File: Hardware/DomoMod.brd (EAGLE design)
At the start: 80 x 30 mm, 9 parts, among them Q1 BSS138, Q2 BSS138

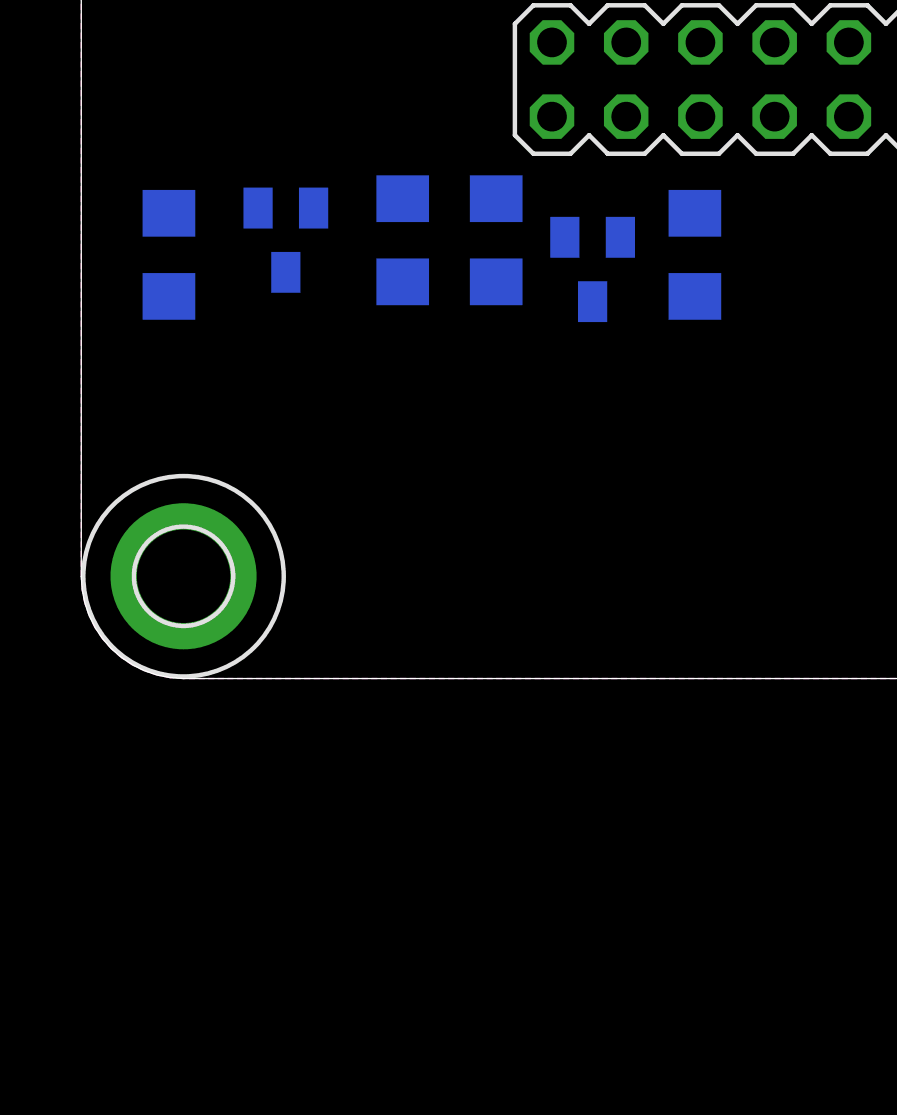
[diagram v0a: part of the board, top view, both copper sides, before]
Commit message: Added schematics for Temp/Hum and barometric pressure sensor.
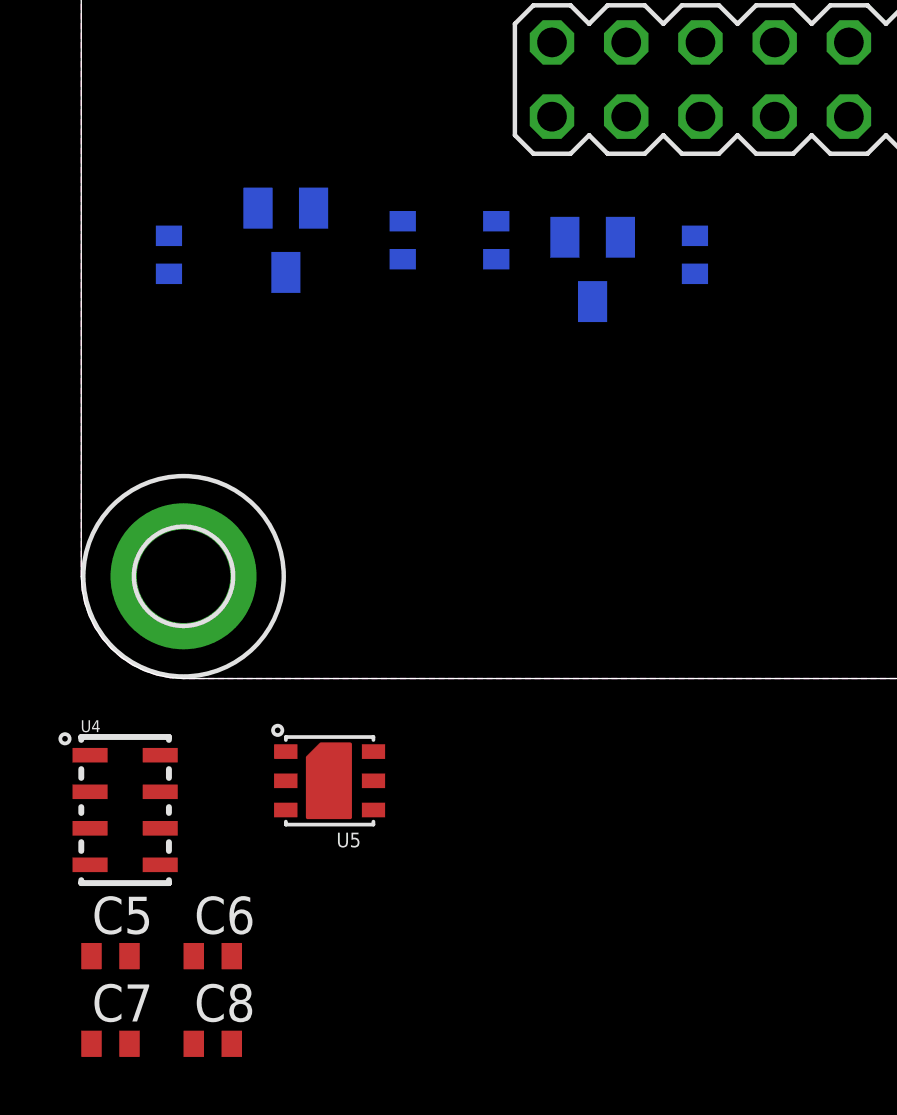
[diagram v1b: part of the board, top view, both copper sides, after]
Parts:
- added C5, C6, C7: 0.1uF, resistor:C0402
- added C8: 1.0uF, resistor:C0402
- added U4: MPL3115A2LGA8, SparkFun-Sensors:LGA8
- added U5: SI7021, SparkFun-Sensors:SI7021
- R1, R2, R3, R4: device resistor:R1206 -> resistor:R0402
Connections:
- new net N$5: C6.1, U4.2
- net 3.3V: now also C5.1, C7.1, C8.1, U4.1, U4.4, U5.VDD
- net GND: now also C5.2, C6.2, C7.2, C8.2, U4.3, U5.GND
- net SCL: now also U4.8, U5.SCK
- net SDA: now also U4.7, U5.DATA
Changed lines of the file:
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@@
 <elements>
 <element name="Q1" library="adafruit" package="SOT23" value="BSS138" x="17.5" y="14" rot="MR180"/>
-<element name="R3" library="resistor" package="R1206" value="10k" x="21" y="14.5" rot="MR270"/>
-<element name="R4" library="resistor" package="R1206" value="10k" x="14.2" y="15" rot="MR90"/>
+<element name="R3" library="resistor" package="R0402" value="10k" x="21" y="14.5" rot="MR270"/>
+<element name="R4" library="resistor" package="R0402" value="10k" x="14.2" y="15" rot="MR90"/>
 <element name="Q2" library="adafruit" package="SOT23" value="BSS138" x="7" y="15" rot="MR180"/>
-<element name="R1" library="resistor" package="R1206" value="10k" x="11" y="15" rot="MR90"/>
-<element name="R2" library="resistor" package="R1206" value="10k" x="3" y="14.5" rot="MR90"/>
+<element name="R1" library="resistor" package="R0402" value="10k" x="11" y="15" rot="MR90"/>
+<element name="R2" library="resistor" package="R0402" value="10k" x="3" y="14.5" rot="MR90"/>
 <element name="H1" library="holes" package="3,2-PAD" value="" x="3.5" y="3.5"/>
 <element name="H2" library="holes" package="3,2-PAD" value="" x="76.5" y="3.5"/>
@@
 <attribute name="MF" value="" x="25" y="20.5" size="1.778" layer="27" display="off"/>
 <attribute name="OC_FARNELL" value="unknown" x="25" y="20.5" size="1.778" layer="27" display="off"/>
+</element>
+<element name="U4" library="SparkFun-Sensors" package="LGA8" value="MPL3115A2LGA8" x="1.5" y="-4.5">
+<attribute name="PROD_ID" value="IC-10869" x="-3" y="3" size="1.778" layer="27" display="off"/>
+</element>
+<element name="C7" library="resistor" package="C0402" value="0.1uF" x="1" y="-12.5"/>
+<element name="C6" library="resistor" package="C0402" value="0.1uF" x="4.5" y="-9.5"/>
+<element name="C8" library="resistor" package="C0402" value="1.0uF" x="4.5" y="-12.5"/>
+<element name="C5" library="resistor" package="C0402" value="0.1uF" x="1" y="-9.5"/>
+<element name="U5" library="SparkFun-Sensors" package="SI7021" value="SI7021" x="8.5" y="-3.5" rot="R180">
+<attribute name="PROD_ID" value="IC-13093" x="23" y="3" size="1.778" layer="27" rot="R180" display="off"/>
 </element>
 </elements>
@@
 <contactref element="SV2" pad="14"/>
 <contactref element="SV2" pad="16"/>
+<contactref element="U4" pad="3"/>
+<contactref element="U5" pad="GND"/>
+<contactref element="U4" pad="3"/>
+<contactref element="C6" pad="2"/>
+<contactref element="C8" pad="2"/>
+<contactref element="C7" pad="2"/>
+<contactref element="U5" pad="GND"/>
+<contactref element="C5" pad="2"/>
 <wire x1="33.89" y1="21.77" x2="76.5" y2="3.5" width="0" layer="19" extent="1-1"/>
 <wire x1="31.35" y1="21.77" x2="33.89" y2="21.77" width="0" layer="19" extent="1-1"/>
 <wire x1="3.5" y1="3.5" x2="31.35" y2="21.77" width="0" layer="19" extent="1-1"/>
+<wire x1="7" y1="-3.5" x2="3.5" y2="3.5" width="0" layer="19" extent="1-1"/>
+<wire x1="5.15" y1="-9.5" x2="7" y2="-3.5" width="0" layer="19" extent="1-1"/>
+<wire x1="5.15" y1="-12.5" x2="5.15" y2="-9.5" width="0" layer="19" extent="1-1"/>
+<wire x1="1.65" y1="-12.5" x2="5.15" y2="-12.5" width="0" layer="19" extent="1-1"/>
+<wire x1="1.65" y1="-9.5" x2="1.65" y2="-12.5" width="0" layer="19" extent="1-1"/>
+<wire x1="0.3" y1="-5.125" x2="1.65" y2="-9.5" width="0" layer="19" extent="1-1"/>
 </signal>
 <signal name="VCC">
@@
 <contactref element="R2" pad="2"/>
 <contactref element="SV2" pad="15"/>
-<wire x1="14.2" y1="16.422" x2="3" y2="15.922" width="0" layer="19" extent="16-16"/>
-<wire x1="33.89" y1="19.23" x2="3" y2="15.922" width="0" layer="19" extent="16-16"/>
+<wire x1="14.2" y1="15.65" x2="3" y2="15.15" width="0" layer="19" extent="16-16"/>
+<wire x1="33.89" y1="19.23" x2="3" y2="15.15" width="0" layer="19" extent="16-16"/>
 </signal>
 <signal name="D2">
@@
 <contactref element="R2" pad="1"/>
 <contactref element="SV2" pad="4"/>
-<wire x1="7" y1="13.9" x2="3" y2="13.078" width="0" layer="19" extent="16-16"/>
+<wire x1="7" y1="13.9" x2="3" y2="13.85" width="0" layer="19" extent="16-16"/>
 <wire x1="18.65" y1="21.77" x2="7" y2="13.9" width="0" layer="19" extent="16-16"/>
 </signal>
@@
 <contactref element="R4" pad="1"/>
 <contactref element="SV2" pad="3"/>
-<wire x1="17.5" y1="12.9" x2="14.2" y2="13.578" width="0" layer="19" extent="16-16"/>
+<wire x1="17.5" y1="12.9" x2="14.2" y2="14.35" width="0" layer="19" extent="16-16"/>
 <wire x1="18.65" y1="19.23" x2="17.5" y2="12.9" width="0" layer="19" extent="16-16"/>
 </signal>
 <signal name="3.3V">
+<contactref element="R1" pad="2"/>
+<contactref element="SV2" pad="13"/>
+<contactref element="U5" pad="VDD"/>
+<contactref element="U4" pad="1"/>
+<contactref element="U4" pad="4"/>
+<contactref element="C8" pad="1"/>
+<contactref element="C7" pad="1"/>
+<contactref element="C5" pad="1"/>
+<contactref element="Q2" pad="1"/>
 <contactref element="R3" pad="2"/>
 <contactref element="Q1" pad="1"/>
-<contactref element="R1" pad="2"/>
-<contactref element="Q2" pad="1"/>
-<contactref element="SV2" pad="13"/>
-<wire x1="6.05" y1="16.1" x2="11" y2="16.422" width="0" layer="19" extent="16-16"/>
-<wire x1="21" y1="13.078" x2="11" y2="16.422" width="0" layer="19" extent="16-16"/>
-<wire x1="16.55" y1="15.1" x2="21" y2="13.078" width="0" layer="19" extent="16-16"/>
-<wire x1="31.35" y1="19.23" x2="16.55" y2="15.1" width="0" layer="19" extent="16-16"/>
+<wire x1="21" y1="13.85" x2="31.35" y2="19.23" width="0" layer="19" extent="16-16"/>
+<wire x1="16.55" y1="15.1" x2="21" y2="13.85" width="0" layer="19" extent="16-16"/>
+<wire x1="11" y1="15.65" x2="16.55" y2="15.1" width="0" layer="19" extent="16-16"/>
+<wire x1="6.05" y1="16.1" x2="11" y2="15.65" width="0" layer="19" extent="16-16"/>
+<wire x1="10" y1="-3.5" x2="6.05" y2="16.1" width="0" layer="19" extent="1-16"/>
+<wire x1="0.3" y1="-2.625" x2="10" y2="-3.5" width="0" layer="19" extent="1-1"/>
+<wire x1="0.3" y1="-6.375" x2="0.3" y2="-2.625" width="0" layer="19" extent="1-1"/>
+<wire x1="0.35" y1="-9.5" x2="0.3" y2="-6.375" width="0" layer="19" extent="1-1"/>
+<wire x1="0.35" y1="-12.5" x2="0.35" y2="-9.5" width="0" layer="19" extent="1-1"/>
+<wire x1="3.85" y1="-12.5" x2="0.35" y2="-12.5" width="0" layer="19" extent="1-1"/>
 </signal>
 <signal name="SDA">
 <contactref element="Q2" pad="2"/>
 <contactref element="R1" pad="1"/>
-<wire x1="7.95" y1="16.1" x2="11" y2="13.578" width="0" layer="19" extent="16-16"/>
+<contactref element="U4" pad="7"/>
+<contactref element="U5" pad="DATA"/>
+<wire x1="11" y1="14.35" x2="7.95" y2="16.1" width="0" layer="19" extent="16-16"/>
+<wire x1="7" y1="-2.5" x2="11" y2="14.35" width="0" layer="19" extent="1-16"/>
+<wire x1="2.7" y1="-3.875" x2="7" y2="-2.5" width="0" layer="19" extent="1-1"/>
 </signal>
 <signal name="SCL">
 <contactref element="Q1" pad="2"/>
 <contactref element="R3" pad="1"/>
-<wire x1="18.45" y1="15.1" x2="21" y2="15.922" width="0" layer="19" extent="16-16"/>
+<contactref element="U4" pad="8"/>
+<contactref element="U5" pad="SCK"/>
+<wire x1="18.45" y1="15.1" x2="21" y2="15.15" width="0" layer="19" extent="16-16"/>
+<wire x1="10" y1="-2.5" x2="18.45" y2="15.1" width="0" layer="19" extent="1-16"/>
+<wire x1="2.7" y1="-2.625" x2="10" y2="-2.5" width="0" layer="19" extent="1-1"/>
 </signal>
 <signal name="A1">
@@
 <contactref element="SV2" pad="2"/>
 </signal>
+<signal name="N$5">
+<contactref element="U4" pad="2"/>
+<contactref element="C6" pad="1"/>
+<wire x1="0.3" y1="-3.875" x2="3.85" y2="-9.5" width="0" layer="19" extent="1-1"/>
+</signal>
 </signals>

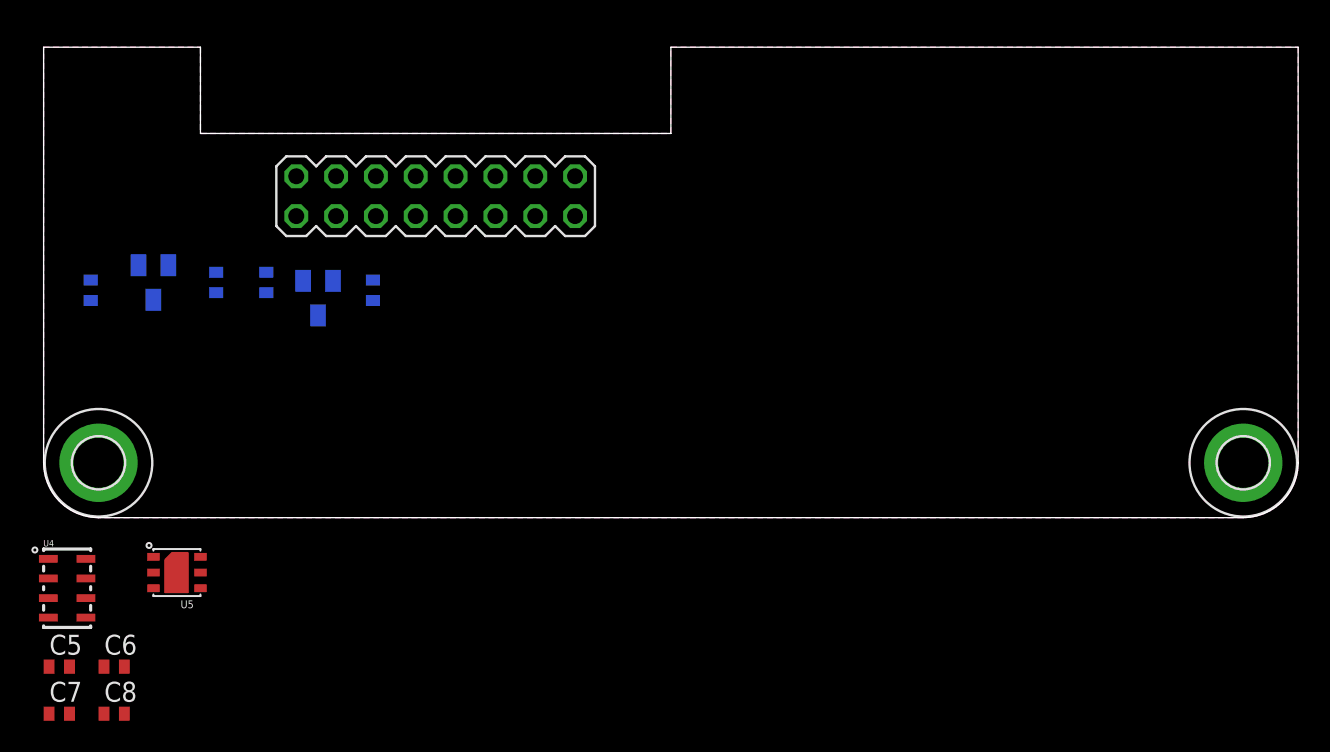
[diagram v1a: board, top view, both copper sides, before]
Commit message: SCH: -Components placed and connected -Documented BRD: -Components placed -100% routed -DRC passed
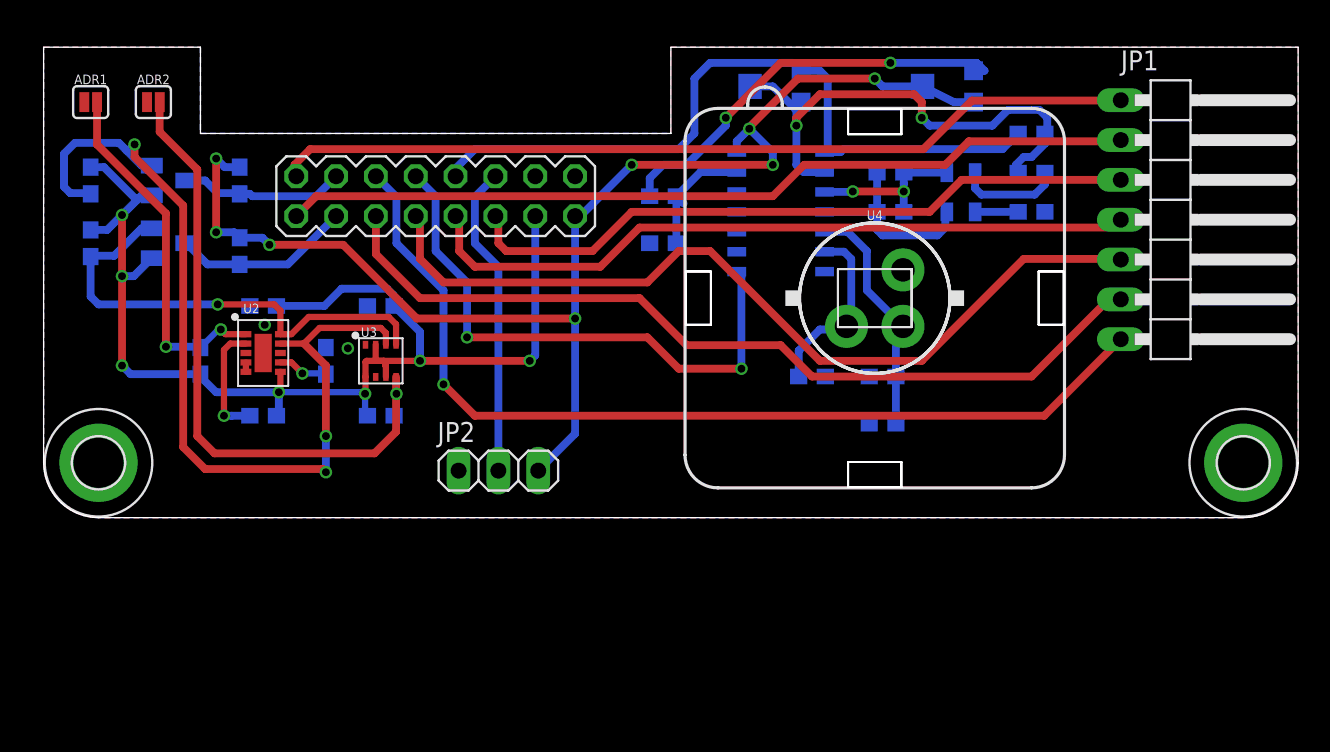
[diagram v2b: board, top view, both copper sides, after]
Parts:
- removed U5: SI7021, SparkFun-Sensors:SI7021
- added ADR1, ADR2: (no value), SparkFun-Jumpers:SMT-JUMPER_2_NO_SILK
- added C1, C9: 0.1uF, SparkFun-Capacitors:0603
- added C2: 1.0uF, SparkFun-Capacitors:0603
- added C3: 22uF, SparkFun-Capacitors:0805
- added C4: 10nF, SparkFun-Capacitors:0603
- added JP1: (no value), pinhead:1X07/90
- added JP2: (no value), pinhead:1X03
- added R10, R12: 10k, SparkFun-Resistors:0603
- added R11: 560k, openPIR-temp:0603
- added R13, R14: 1M, openPIR-temp:TRIMPOT-TC33X
- added R15: 51k, openPIR-temp:0603
- added R5: 4.7k, SparkFun-Resistors:0603
- added R6, R7, R8: 100k, SparkFun-Resistors:0603
- added R9: 43k, SparkFun-Resistors:0603
- added U$1: CWM 0.5 GI V1, openPIR-temp:LENS-CWM-0.5-GI-V1
- added U1: NCS36000, openPIR-temp:SO14
- added U2: CCS811, SparkFun-Sensors:LGA10
- added U3: BME280, SparkFun-Sensors:LGA-8-2.5X2.5
- C5, C6: device resistor:C0402 -> SparkFun-Capacitors:0603
- C7: value 0.1uF -> 22uF; device resistor:C0402 -> SparkFun-Capacitors:0805
- C8: value 1.0uF -> 10nF; device resistor:C0402 -> SparkFun-Capacitors:0603
- R1, R2, R3, R4: device resistor:R0402 -> SparkFun-Resistors:0603
- U4: value MPL3115A2LGA8 -> PIR; device SparkFun-Sensors:LGA8 -> openPIR-temp:PIR
- moved C8 69.2 mm to (63.0, 24.5), flipped to the bottom
- moved C7 67.1 mm to (58.5, 22.0), flipped to the bottom, turned to 180 degrees
- moved C5 55.7 mm to (53.5, 9.00), flipped to the bottom
- moved U4 54.7 mm to (53.0, 14.0)
- moved C6 48.2 mm to (49.0, 9.00), flipped to the bottom, turned to 180 degrees
- moved R3 18.2 mm to (3.00, 17.5), turned to 90 degrees
- moved R2 11.8 mm to (12.5, 21.5)
- moved R1 10.3 mm to (3.00, 21.5)
- moved Q1 10.1 mm to (8.00, 17.5), turned to 90 degrees
- moved Q2 6.58 mm to (8.00, 21.5), turned to 90 degrees
- moved R4 2.62 mm to (12.5, 17.0)
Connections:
- new net !RST: R5.1, U2.2
- new net !WAKE: R8.2, U2.7
- new net CCS811_ADDR: ADR1.2, R6.1, U2.1
- new net N$1: C5.1, R9.2, U1.5, U4.S
- new net N$11: R14.1, R15.2
- new net N$2: C6.1, U1.6, U4.D
- new net N$3: C3.2, R10.2
- new net N$4: C7.2, R12.2
- new net N$6: C4.1, C7.1, R11.2, U1.3
- new net N$7: C8.1, R12.1, R13.2, R13.3, U1.2
- new net N$8: C9.1, R15.1, U1.13
- new net NTC_SENSE: U2.4, U2.5
- new net SDO/ADR: ADR2.2, R7.1, U3.5
- net 3.3V: now also C1.1, C2.1, R5.2, R6.2, R7.2, U2.6, U3.2, U3.6, U3.8; no longer C5.1, C7.1, C8.1, U4.1, U4.4, U5.VDD
- net A1: now also JP2.2
- net A2: now also C8.2, R13.1, U1.1
- net A3: now also U1.8
- net A4: now also JP1.7
- net D0: now also JP1.1
- net D1: now also JP1.2
- net D5: now also JP1.3
- net D6: now also JP1.4
- net D7: now also JP1.5
- net D8: now also JP1.6
- net GND: now also ADR1.1, ADR2.1, C1.2, C2.2, C9.2, JP2.1, R10.1, R8.1, R9.1, U1.7, U2.EP, U3.1, U3.7, U4.G; no longer C7.2, C8.2, U4.3, U5.GND
- net N$5: now also C3.1, C4.2, R11.1, U1.4; no longer C6.1, U4.2
- net SCL: now also U2.10, U3.4; no longer U4.8, U5.SCK
- net SDA: now also U2.9, U3.3; no longer U4.7, U5.DATA
- net VCC: now also JP2.3, R14.2, R14.3, U1.14
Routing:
- net VCC: track 0.00 -> 83.8 mm, vias 0 -> 8
- net 3.3V: track 0.00 -> 78.9 mm, vias 0 -> 7
- net A4: track 0.00 -> 61.3 mm, vias 0 -> 1
- net SDA: track 0.00 -> 58.3 mm, vias 0 -> 3
- net D8: track 0.00 -> 55.3 mm
- net D0: track 0.00 -> 55.2 mm
- net D7: track 0.00 -> 54.6 mm
- net D1: track 0.00 -> 54.6 mm
- net A2: track 0.00 -> 47.1 mm
- net D6: track 0.00 -> 46.2 mm
- net D5: track 0.00 -> 43.6 mm
- net SDO/ADR: track 0.00 -> 42.0 mm, vias 0 -> 1
- net A3: track 0.00 -> 36.3 mm, vias 0 -> 2
- net N$7: track 0.00 -> 33.5 mm, vias 0 -> 2
- net SCL: track 0.00 -> 30.5 mm, vias 0 -> 1
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
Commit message: Update
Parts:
- removed JP1: (no value), pinhead:1X07/90
- removed JP2: (no value), pinhead:1X03
- added JP3, JP4, JP5, JP6: (no value), pinhead:1X02
- added JP7: (no value), pinhead:1X03
- added JP8: (no value), pinhead:1X04
- added R16: 1k, SparkFun-Resistors:0603
- added R17, R18, R19: 10k, SparkFun-Resistors:0603
- added T1: MMBT2222A, transistor:SOT23-BEC
- moved ADR1 1.30 mm to (3.00, 27.8), flipped to the bottom, turned to 180 degrees
- moved ADR2 1.30 mm to (7.00, 27.8), flipped to the bottom, turned to 180 degrees
- turned C4 to 180 degrees
- turned R10 to 180 degrees
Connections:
- new net N$10: R16.1, T1.B
- new net N$9: JP3.2, T1.C
- net A1: now also JP4.2, R17.2; no longer JP2.2
- net A3: now also JP6.2, R19.2; no longer U1.8
- net A4: now also JP5.2, R18.2; no longer JP1.7
- net D0: no longer JP1.1
- net D1: no longer JP1.2
- net D2: now also JP8.2
- net D3: now also JP8.1
- net D5: now also JP7.1; no longer JP1.3
- net D6: now also R16.2; no longer JP1.4
- net D7: now also JP6.1; no longer JP1.5
- net D8: now also U1.8; no longer JP1.6
- net GND: now also JP7.3, JP8.4, R17.1, R18.1, R19.1, T1.E; no longer JP2.1
- net N$4: now also R12.1; no longer R12.2
- net N$5: now also C4.1; no longer C4.2
- net N$6: now also C4.2; no longer C4.1
- net N$7: now also R12.2; no longer R12.1
- net VCC: now also JP3.1, JP4.1, JP5.1, JP7.2, JP8.3; no longer JP2.3
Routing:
- net D2: track 10.5 -> 149.8 mm, vias 0 -> 1
- net D3: track 11.4 -> 113.3 mm
- net D1: track 54.6 -> 0.00 mm
- net A1: track 19.9 -> 73.9 mm, vias 0 -> 2
- net A3: track 36.3 -> 64.3 mm, vias 2 -> 1
- net VCC: track 83.8 -> 110.7 mm
- net D8: track 55.3 -> 31.2 mm, vias 0 -> 2
- net A4: track 61.3 -> 75.5 mm, vias 1 -> 4
- net D0: track 55.2 -> 41.3 mm
- net N$9: track 0.00 -> 10.9 mm
- net D7: track 54.6 -> 62.1 mm
- net D5: track 43.6 -> 49.3 mm
- net CCS811_ADDR: track 23.1 -> 28.0 mm, vias 2 -> 3
- net N$3: track 2.75 -> 6.78 mm
- net N$4: track 6.63 -> 2.75 mm
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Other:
- board text added: "+"
- board text added: "-"
- board text added: "-CO -TVOC"
- board text added: "-Temp -Pres -Hum"
- board text added: "2"
- board text added: "ACCES"
- board text added: "Environment Conditions"
- board text added: "LDR"
- board text added: "LED"
- board text added: "MOISTURE"
- board text added: "NTC"
- board text added: "Presence sensor"
- board text added: "S"
- board text added: "SCL"
- board text added: "SDA"
- board text added: "SERVO"
